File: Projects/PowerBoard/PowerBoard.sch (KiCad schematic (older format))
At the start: 1 part

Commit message: Added a part
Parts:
- removed U?: 74469, symbol 74469
- added U?: ATX_Power_Connector, symbol ATX_Power_Connector
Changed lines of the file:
@@
 LIBS:contrib
 LIBS:valves
+LIBS:USSTComponents
+LIBS:TomParts
+LIBS:PowerBoard-cache
 EELAYER 25 0
 EELAYER END
@@
 $EndDescr
 $Comp
-L 74469 U?
-U 1 1 56913B96
-P 2600 2150
-F 0 "U?" H 2600 2150 70  0000 C CNN
-F 1 "74469" H 2600 1950 70  0000 C CNN
-F 2 "" H 2600 2150 60  0000 C CNN
-F 3 "" H 2600 2150 60  0000 C CNN
-	1    2600 2150
+L ATX_Power_Connector U?
+U 1 1 56913D73
+P 3200 3450
+F 0 "U?" H 3700 3650 60  0000 C CNN
+F 1 "ATX_Power_Connector" H 3700 3650 60  0000 C CNN
+F 2 "" H 3700 3650 60  0000 C CNN
+F 3 "" H 3700 3650 60  0000 C CNN
+	1    3200 3450
 	1    0    0    -1
 $EndComp

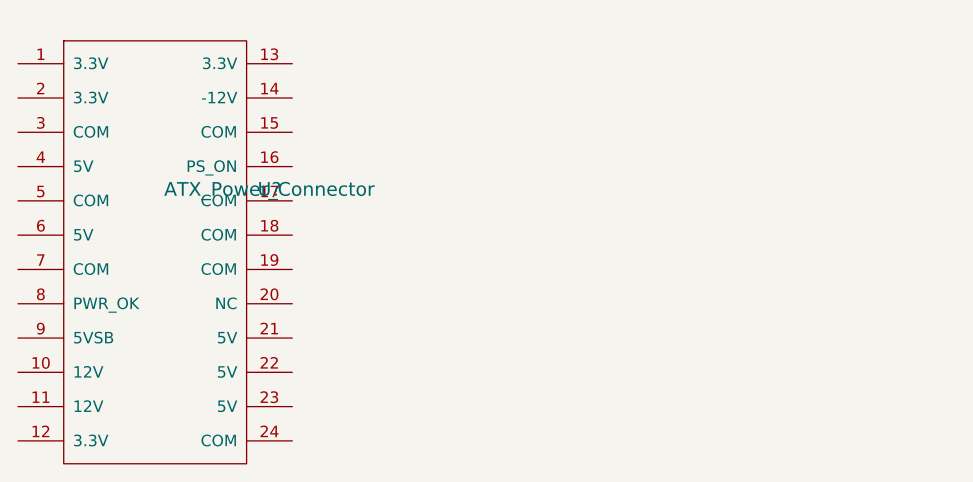
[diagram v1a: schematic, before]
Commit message: Created the ATX Connector
Located in the “TomParts” Library
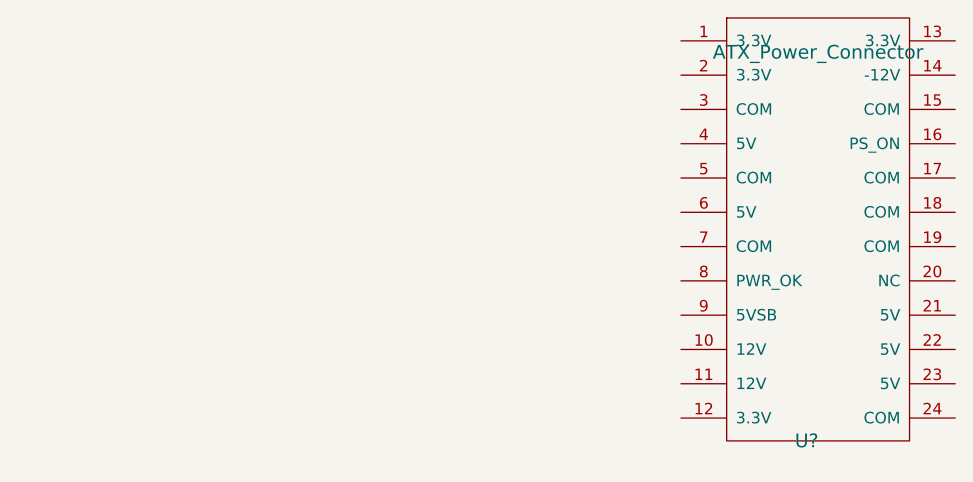
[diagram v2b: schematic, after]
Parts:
- removed U?: ATX_Power_Connector, symbol ATX_Power_Connector
- added U?: ATX_Power_Connector, symbol ATX_Power_Connector
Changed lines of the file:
@@
 $Comp
 L ATX_Power_Connector U?
-U 1 1 56913D73
-P 3200 3450
-F 0 "U?" H 3700 3650 60  0000 C CNN
-F 1 "ATX_Power_Connector" H 3700 3650 60  0000 C CNN
-F 2 "" H 3700 3650 60  0000 C CNN
-F 3 "" H 3700 3650 60  0000 C CNN
-	1    3200 3450
+U 1 1 569412F8
+P 6100 3350
+F 0 "U?" H 6050 2350 60  0000 C CNN
+F 1 "ATX_Power_Connector" H 6100 4050 60  0000 C CNN
+F 2 "" H 6600 3550 60  0000 C CNN
+F 3 "" H 6600 3550 60  0000 C CNN
+	1    6100 3350
 	1    0    0    -1
 $EndComp

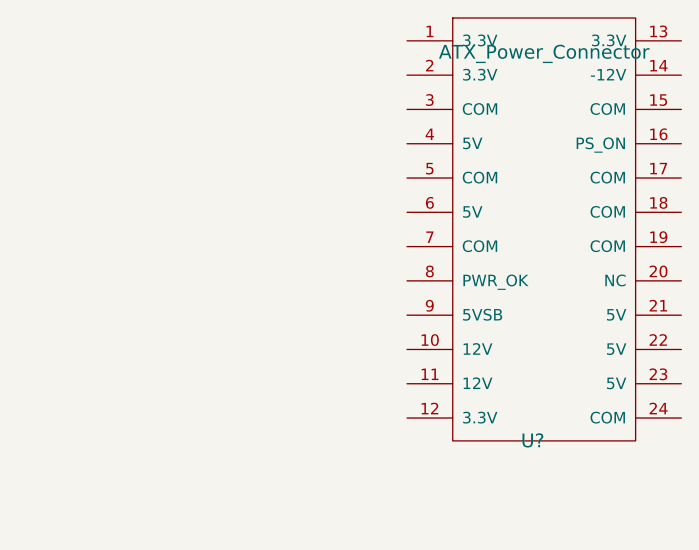
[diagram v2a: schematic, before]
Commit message: Added a Vcc and a GND to the diagram
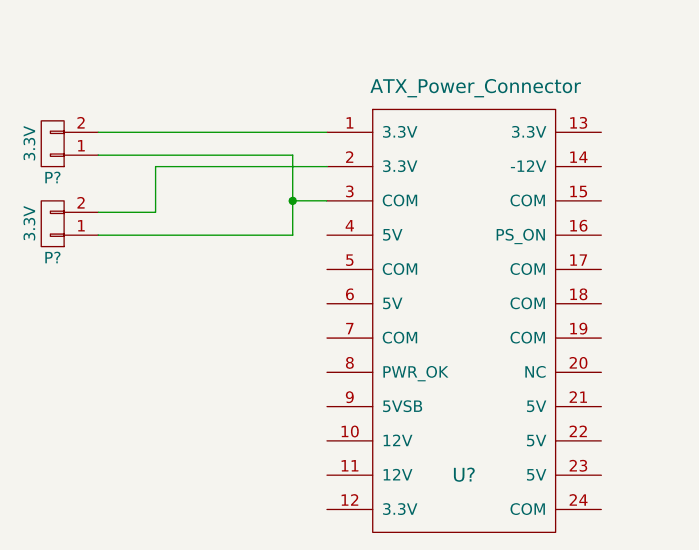
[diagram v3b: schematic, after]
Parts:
- removed U?: ATX_Power_Connector, symbol ATX_Power_Connector
- added P? (x2): 3.3V, symbol CONN_01X02
- added U?: ATX_Power_Connector, symbol ATX_Power_Connector
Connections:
- new net: P?.2 (P2), U?.1 (3.3V)
- new net: P?.2 (P2), U?.2 (3.3V)
- new net: P?.1 (P1), P?.1 (P1), U?.3 (COM)
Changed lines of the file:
@@
 $Comp
 L ATX_Power_Connector U?
-U 1 1 569412F8
-P 6100 3350
-F 0 "U?" H 6050 2350 60  0000 C CNN
-F 1 "ATX_Power_Connector" H 6100 4050 60  0000 C CNN
-F 2 "" H 6600 3550 60  0000 C CNN
-F 3 "" H 6600 3550 60  0000 C CNN
-	1    6100 3350
+U 1 1 56941546
+P 5750 3750
+F 0 "U?" H 5750 3000 60  0000 C CNN
+F 1 "ATX_Power_Connector" H 5800 4700 60  0000 C CNN
+F 2 "" H 6300 4200 60  0000 C CNN
+F 3 "" H 6300 4200 60  0000 C CNN
+	1    5750 3750
 	1    0    0    -1
 $EndComp
+$Comp
+L CONN_01X02 P?
+U 1 1 56941663
+P 3950 3050
+F 0 "P?" H 3950 3200 50  0000 C CNN
+F 1 "3.3V" V 4050 3050 50  0000 C CNN
+F 2 "" H 3950 3050 60  0000 C CNN
+F 3 "" H 3950 3050 60  0000 C CNN
+	1    3950 3050
+	-1   0    0    1
+$EndComp
+Wire Wire Line
+	5150 3000 4150 3000
+Wire Wire Line
+	4150 3100 5000 3100
+Wire Wire Line
+	5000 3100 5000 3300
+Wire Wire Line
+	5000 3300 5000 3450
+Wire Wire Line
+	5000 3300 5150 3300
+$Comp
+L CONN_01X02 P?
+U 1 1 56941795
+P 3950 3400
+F 0 "P?" H 3950 3550 50  0000 C CNN
+F 1 "3.3V" V 4050 3400 50  0000 C CNN
+F 2 "" H 3950 3400 60  0000 C CNN
+F 3 "" H 3950 3400 60  0000 C CNN
+	1    3950 3400
+	-1   0    0    1
+$EndComp
+Wire Wire Line
+	4400 3150 5150 3150
+Wire Wire Line
+	4400 3150 4400 3350
+Wire Wire Line
+	4400 3350 4150 3350
+Wire Wire Line
+	5000 3450 4150 3450
+Connection ~ 5000 3300
 $EndSCHEMATC

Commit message: Created More Parts
Switching Regulator
Op-Amp (LT1636)
Made changes to the Power Board
by adding more connections
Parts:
- added P? (x2): 3.3V, symbol CONN_01X02
- added P? (x5): 5V, symbol CONN_01X02
- added P? (x2): 12V, symbol CONN_01X02
- added P?: 24V In, symbol CONN_01X02
- U?: symbol ATX_Power_Connector -> ATX_Power_Connector-RESCUE-PowerBoard
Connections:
- net labels added: +24V, GND
- wire segments 9 -> 55
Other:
- moved on the sheet: P?, U?

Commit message: Changes to High Power Circuit
Added a bunch of changes that can be seen on the change log
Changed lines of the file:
@@
 $EndComp
 $Comp
-L GND #PWR?
+L GND-RESCUE-PowerBoard #PWR?
 U 1 1 569D92A5
 P 1200 7450
